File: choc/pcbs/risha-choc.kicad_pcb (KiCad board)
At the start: 2 copper layers, 100 x 85 mm, 23 parts

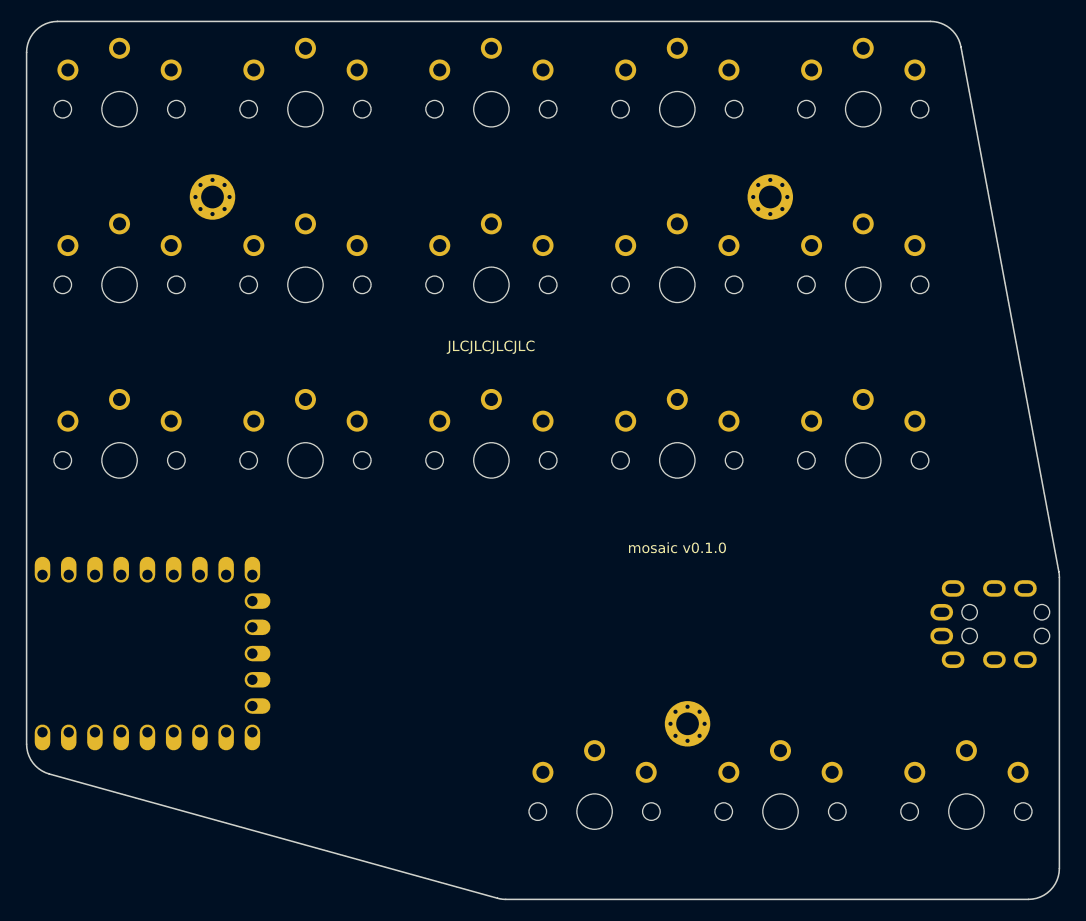
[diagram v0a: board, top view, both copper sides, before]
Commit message: rename; choc and MX versions
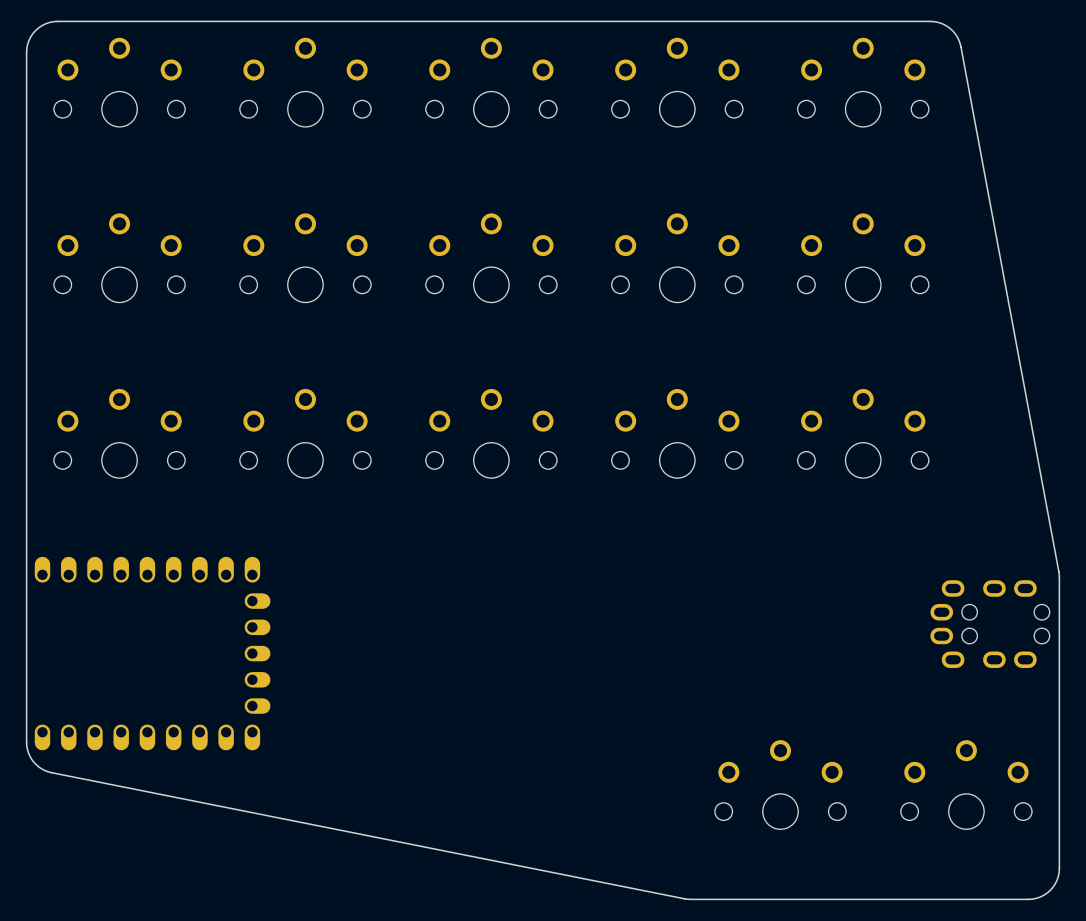
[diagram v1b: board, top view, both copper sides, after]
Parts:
- removed S18: , PG1350
- removed _2, _3, _4: , MountingHole_2.2mm_M2_Pad_Via
- moved S16 18.0 mm to (208.0, 170.0)
- moved S17 18.0 mm to (226.0, 170.0)
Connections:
- ? pad 19: thumbfan_home_home -> thumbfan_far_home
- ? pad 20: thumbfan_far_home -> GP29
- S17 pad 1: thumbfan_home_home -> thumbfan_far_home
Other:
- outline, holes or cut-outs redrawn
- board text removed: "JLCJLCJLCJLC"
- board text removed: "mosaic v0.1.0"

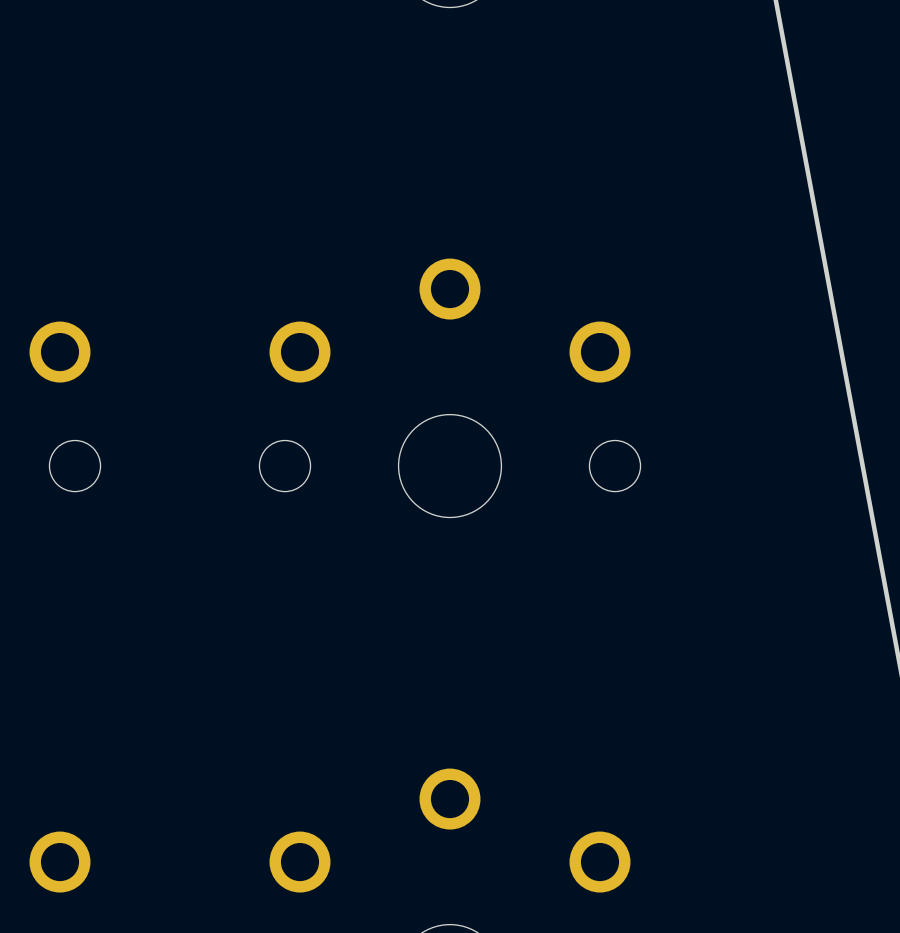
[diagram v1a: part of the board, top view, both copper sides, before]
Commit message: adding version and JLC text
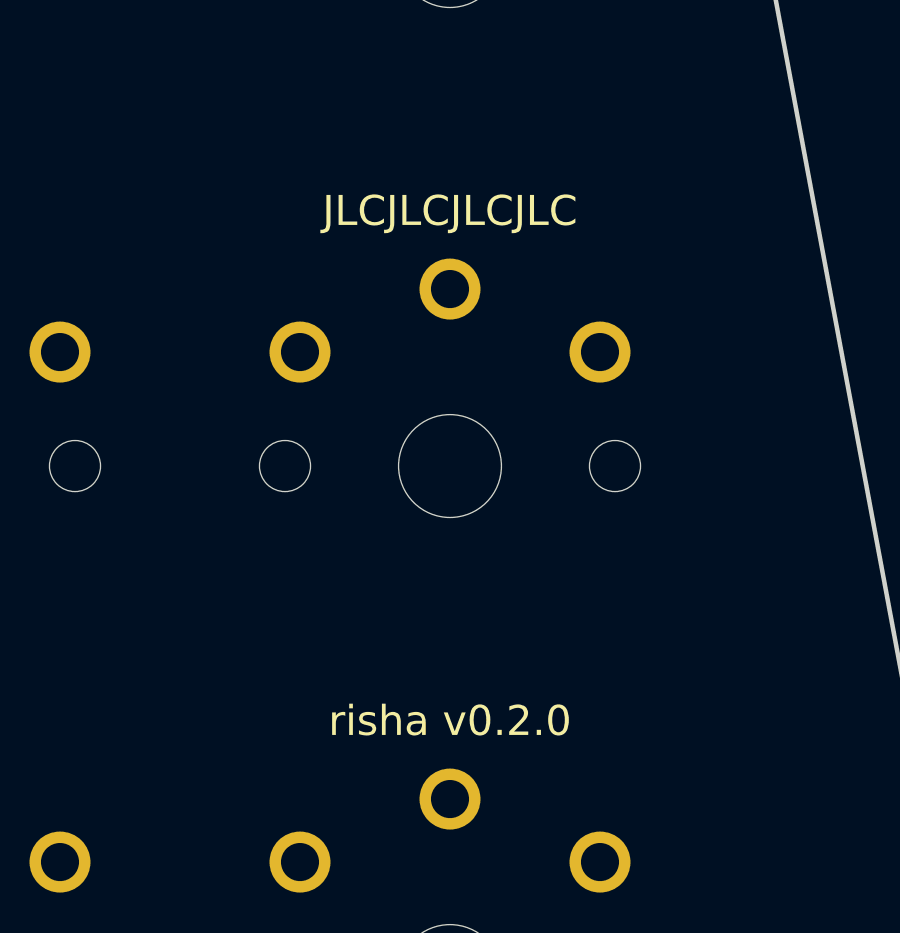
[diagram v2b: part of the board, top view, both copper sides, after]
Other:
- board text added: "JLCJLCJLCJLC"
- board text added: "risha v0.2.0"
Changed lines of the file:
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@@
         (pad 4 thru_hole oval (at -4.6 3.2 270) (size 1.6 2.2) (drill oval 0.9 1.5) (layers *.Cu *.Mask) (net 19 "GP8"))
       )
+            (gr_text "JLCJLCJLCJLC" (at 216 110.5 0) (layer F.SilkS)
+                (effects (font (size 1 1) (thickness 0.15)) )
+            )
+            (gr_text "risha v0.2.0" (at 216 127.5 0) (layer F.SilkS)
+                (effects (font (size 1 1) (thickness 0.15)) )
+            )
             (gr_line (start 135 163.28877844674167) (end 135 96.5) (angle 90) (layer Edge.Cuts) (width 0.15))
 (gr_line (start 138 93.5) (end 222.50790643613448 93.5) (angle 90) (layer Edge.Cuts) (width 0.15))

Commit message: drop mx thumb cluster a little lower
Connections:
- TRRS1 pad 3: GP9 -> GP8
- TRRS1 pad 4: GP8 -> GP9
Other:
- net class Default removed

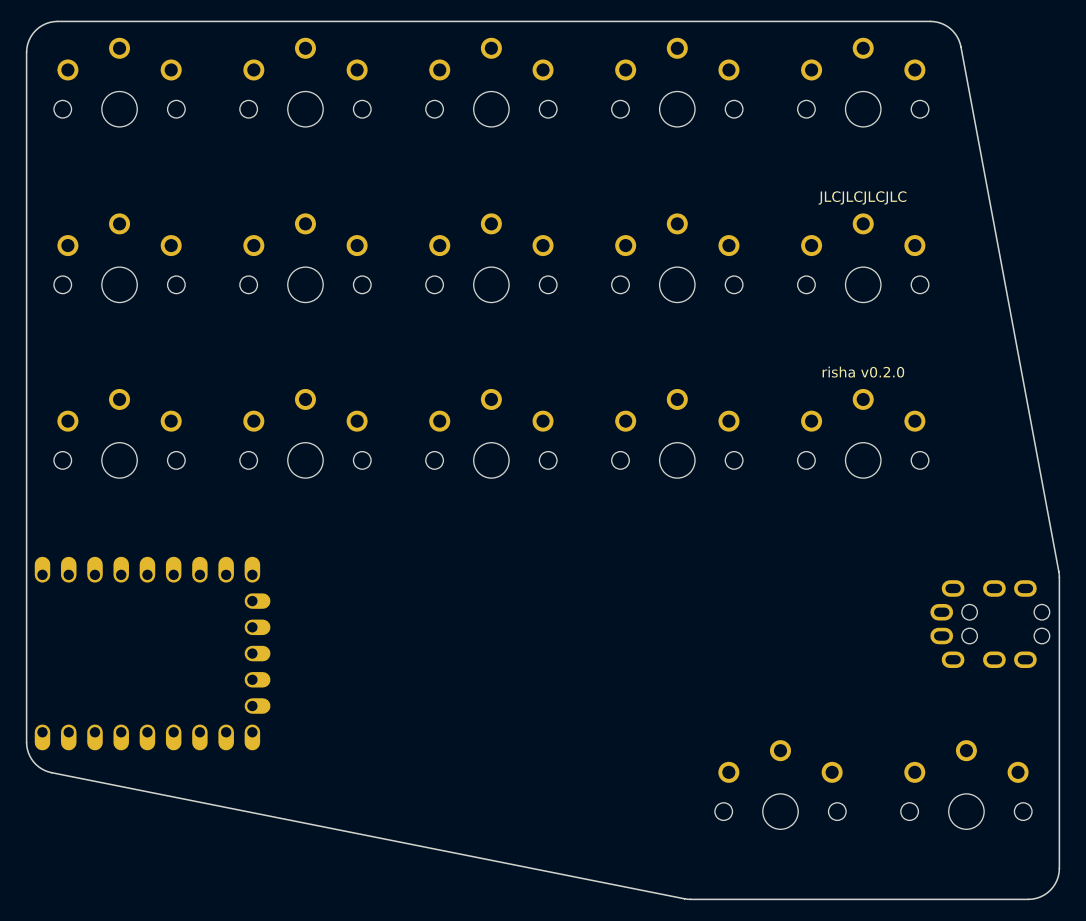
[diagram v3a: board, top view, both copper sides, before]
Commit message: outline tweaks for ergonomics
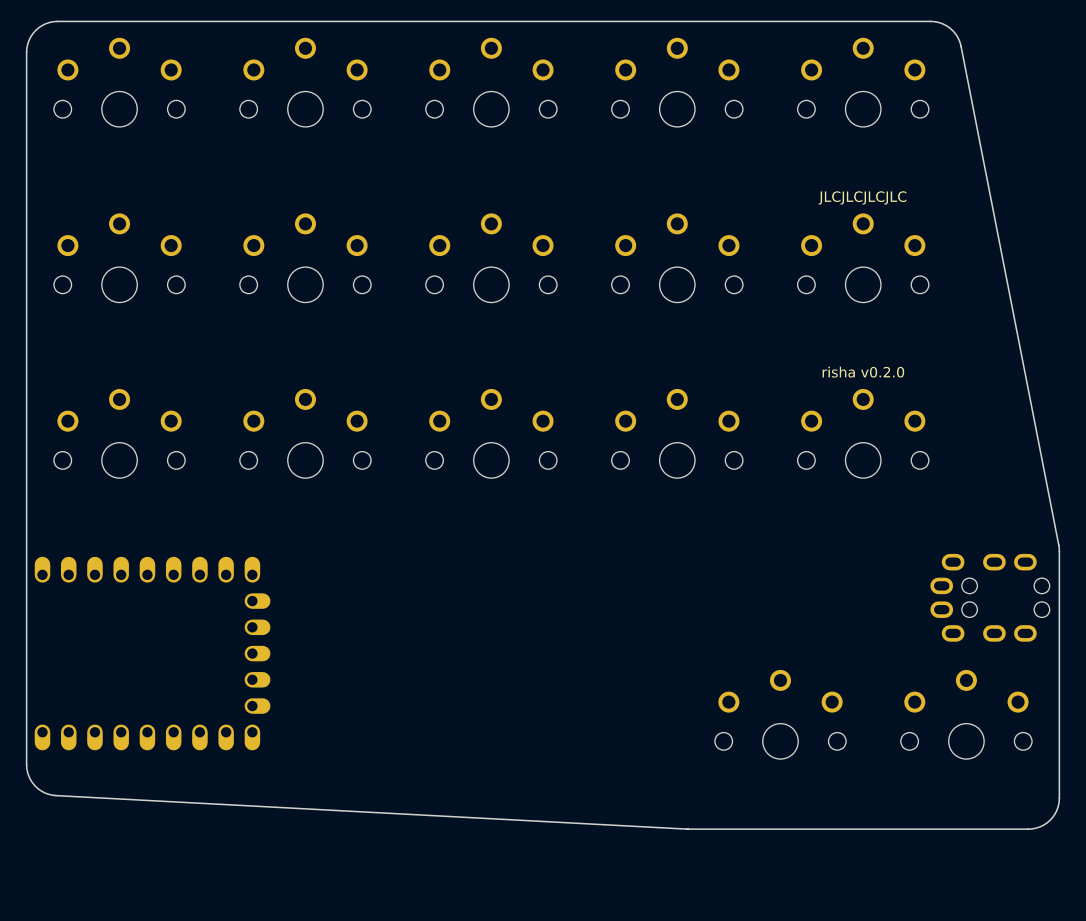
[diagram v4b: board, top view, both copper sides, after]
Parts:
- moved S16 6.80 mm to (208.0, 163.2)
- moved S17 6.80 mm to (226.0, 163.2)
- moved TRRS1 2.55 mm to (234.9, 150.4)
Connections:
- TRRS1 pad 3: GP8 -> GP9
- TRRS1 pad 4: GP9 -> GP8
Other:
- board size 100 x 85 mm -> 100 x 78.2 mm
- net class Default added: clearance 0.2, trace_width 0.25, via_dia 0.8, via_drill 0.4

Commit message: hacky sub 100mm^2 idea for rear-facing trrs
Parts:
- moved TRRS1 7.65 mm to (231.4, 143.7), turned to 0 degrees
- moved S16 2.55 mm to (208.0, 165.8)
- moved S17 2.55 mm to (226.0, 165.8)
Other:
- board size 100 x 78.2 mm -> 100 x 80.8 mm
- board text added: "risha v1.0.0"
- board text removed: "risha v0.2.0"

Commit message: trying new choc outline
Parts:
- added S18: , PG1350, F.Cu at (226.0, 165.8)
- added _4: , MountingHole_2.2mm_M2_Pad_Via, F.Cu at (153.0, 127.5)
- added _5: , MountingHole_2.2mm_M2_Pad_Via, F.Cu at (207.0, 110.5)
- added _6: , MountingHole_2.2mm_M2_Pad_Via, F.Cu at (217.0, 157.2)
- moved TRRS1 50.2 mm to (230.8, 93.5)
- moved S16 18.0 mm to (190.0, 165.8)
- moved S17 18.0 mm to (208.0, 165.8)
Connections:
- ? pad 10: GP9 -> matrix_index_bottom
- ? pad 11: matrix_middle_bottom -> matrix_index_home
- ? pad 13: matrix_index_home -> GP12
- ? pad 14: matrix_index_bottom -> matrix_inner_top
- ? pad 15: matrix_inner_bottom -> matrix_inner_home
- ? pad 16: matrix_inner_home -> matrix_inner_bottom
- ? pad 17: matrix_inner_top -> thumbfan_near_home
- ? pad 18: thumbfan_near_home -> thumbfan_home_home
- ? pad 9: GP8 -> matrix_middle_bottom
- S17 pad 1: thumbfan_far_home -> thumbfan_middle_home
- TRRS1 pad 1: 3V3 -> GND
- TRRS1 pad 3: GP9 -> VSYS
- TRRS1 pad 4: GP8 -> GP16
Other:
- outline, holes or cut-outs redrawn
